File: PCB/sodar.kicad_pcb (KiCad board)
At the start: 2 copper layers, 71 parts, among them J1 Screw_Terminal_01x02, J2 Conn_02x12_Counter_Clockwise, J3 Conn_01x02, U1 TC78H621FNG, U10 TC78H621FNG, U2 TC78H621FNG, U3 TC78H621FNG, U4 TC78H621FNG, U5 TC78H621FNG, U6 TC78H621FNG, U7 TC78H621FNG, U8 TC78H621FNG, U9 TC78H621FNG

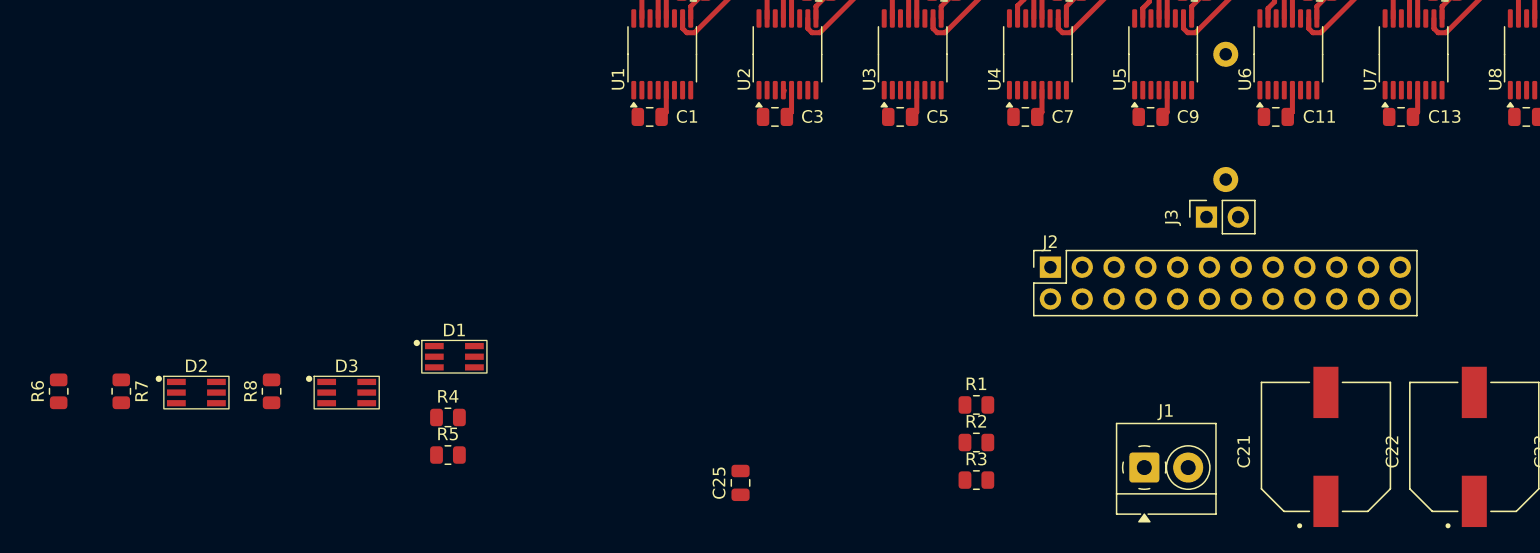
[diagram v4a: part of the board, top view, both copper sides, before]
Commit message: Moved signal connections on the header for easier routing
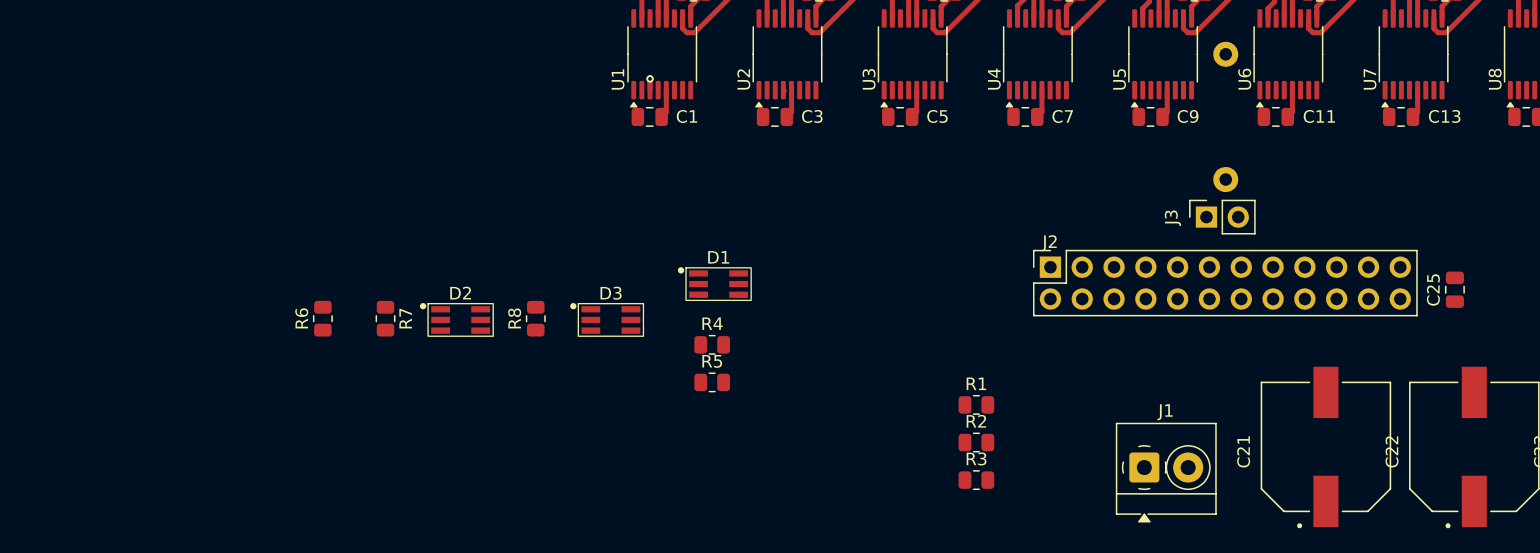
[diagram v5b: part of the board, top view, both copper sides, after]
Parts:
- moved C25 59.1 mm to (168.3, 71.8)
- moved D2 21.9 mm to (88.9, 72.1)
- moved D3 21.9 mm to (100.9, 72.1)
- moved R6 21.9 mm to (77.9, 74.1)
- moved R7 21.9 mm to (82.9, 74.1)
- moved R8 21.9 mm to (94.9, 74.1)
- moved D1 21.9 mm to (109.5, 69.2)
- moved R4 21.9 mm to (109.0, 76.2)
- moved R5 21.9 mm to (109.0, 79.2)
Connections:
- J2 pad 1: S1 -> S2
- J2 pad 10: S10 -> S9
- J2 pad 11: S11 -> S12
- J2 pad 12: S12 -> S11
- J2 pad 13: S13 -> S14
- J2 pad 14: S14 -> S13
- J2 pad 15: S15 -> S16
- J2 pad 16: S16 -> S15
- J2 pad 17: S17 -> S18
- J2 pad 18: S18 -> S17
- J2 pad 2: S2 -> S1
- J2 pad 3: S3 -> S4
- J2 pad 4: S4 -> S3
- J2 pad 5: S5 -> S6
- J2 pad 6: S6 -> S5
- J2 pad 7: S7 -> S8
- J2 pad 8: S8 -> S7
- J2 pad 9: S9 -> S10
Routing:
- net S1: track 0.00 -> 0.90 mm, vias 0 -> 1
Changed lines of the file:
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@@
 	(footprint "footprints:QBLP680-RGB1"
 		(layer "F.Cu")
-		(at 88.4 75.05)
+		(at 109.5 69.25)
 		(property "Reference" "D1"
 			(at 0 0 0)
@@
 	(footprint "Resistor_SMD:R_0805_2012Metric"
 		(layer "F.Cu")
-		(at 56.8 79.9125 90)
+		(at 77.9 74.1125 90)
 		(descr "Resistor SMD 0805 (2012 Metric), square (rectangular) end terminal, IPC_7351 nominal, (Body size source: IPC-SM-782 page 72, https://www.pcb-3d.com/wordpress/wp-content/uploads/ipc-sm-782a_amendment_1_and_2.pdf), generated with kicad-footprint-generator")
 		(tags "resistor")
@@
 	(footprint "Resistor_SMD:R_0805_2012Metric"
 		(layer "F.Cu")
-		(at 61.8 79.9125 -90)
+		(at 82.9 74.1125 -90)
 		(descr "Resistor SMD 0805 (2012 Metric), square (rectangular) end terminal, IPC_7351 nominal, (Body size source: IPC-SM-782 page 72, https://www.pcb-3d.com/wordpress/wp-content/uploads/ipc-sm-782a_amendment_1_and_2.pdf), generated with kicad-footprint-generator")
 		(tags "resistor")
@@
 	(footprint "footprints:QBLP680-RGB1"
 		(layer "F.Cu")
-		(at 79.8 77.9125)
+		(at 100.9 72.1125)
 		(property "Reference" "D3"
 			(at 0 0 0)
@@
 	(footprint "Resistor_SMD:R_0805_2012Metric"
 		(layer "F.Cu")
-		(at 87.8875 82)
+		(at 108.9875 76.2)
 		(descr "Resistor SMD 0805 (2012 Metric), square (rectangular) end terminal, IPC_7351 nominal, (Body size source: IPC-SM-782 page 72, https://www.pcb-3d.com/wordpress/wp-content/uploads/ipc-sm-782a_amendment_1_and_2.pdf), generated with kicad-footprint-generator")
 		(tags "resistor")
@@
 	(footprint "Resistor_SMD:R_0805_2012Metric"
 		(layer "F.Cu")
-		(at 87.8875 85)
+		(at 108.9875 79.2)
 		(descr "Resistor SMD 0805 (2012 Metric), square (rectangular) end terminal, IPC_7351 nominal, (Body size source: IPC-SM-782 page 72, https://www.pcb-3d.com/wordpress/wp-content/uploads/ipc-sm-782a_amendment_1_and_2.pdf), generated with kicad-footprint-generator")
 		(tags "resistor")
@@
 	(footprint "Resistor_SMD:R_0805_2012Metric"
 		(layer "F.Cu")
-		(at 73.8 79.9125 90)
+		(at 94.9 74.1125 90)
 		(descr "Resistor SMD 0805 (2012 Metric), square (rectangular) end terminal, IPC_7351 nominal, (Body size source: IPC-SM-782 page 72, https://www.pcb-3d.com/wordpress/wp-content/uploads/ipc-sm-782a_amendment_1_and_2.pdf), generated with kicad-footprint-generator")
 		(tags "resistor")
@@
 	(footprint "Capacitor_SMD:C_0805_2012Metric"
 		(layer "F.Cu")
-		(at 111.25 87.225 90)
+		(at 168.3 71.8 90)
 		(descr "Capacitor SMD 0805 (2012 Metric), square (rectangular) end terminal, IPC_7351 nominal, (Body size source: IPC-SM-782 page 76, https://www.pcb-3d.com/wordpress/wp-content/uploads/ipc-sm-782a_amendment_1_and_2.pdf, https://docs.google.com/spreadsheets/d/1BsfQQcO9C6DZCsRaXUlFlo91Tg2WpOkGARC1WS5S8t0/edit?usp=sharing), generated with kicad-footprint-generator")
 		(tags "capacitor")
@@
 			(layers "*.Cu" "*.Mask")
 			(remove_unused_layers no)
-			(net 39 "S1")
+			(net 35 "S2")
 			(pinfunction "Pin_1")
 			(pintype "passive")
@@
 			(layers "*.Cu" "*.Mask")
 			(remove_unused_layers no)
-			(net 35 "S2")
+			(net 39 "S1")
 			(pinfunction "Pin_2")
 			(pintype "passive")
@@
 			(layers "*.Cu" "*.Mask")
 			(remove_unused_layers no)
-			(net 42 "S3")
+			(net 38 "S4")
 			(pinfunction "Pin_3")
 			(pintype "passive")
@@
 			(layers "*.Cu" "*.Mask")
 			(remove_unused_layers no)
-			(net 38 "S4")
+			(net 42 "S3")
 			(pinfunction "Pin_4")
 			(pintype "passive")
@@
 			(layers "*.Cu" "*.Mask")
 			(remove_unused_layers no)
-			(net 32 "S5")
+			(net 29 "S6")
 			(pinfunction "Pin_5")
 			(pintype "passive")
@@
 			(layers "*.Cu" "*.Mask")
 			(remove_unused_layers no)
-			(net 29 "S6")
+			(net 32 "S5")
 			(pinfunction "Pin_6")
 			(pintype "passive")
@@
 			(layers "*.Cu" "*.Mask")
 			(remove_unused_layers no)
-			(net 28 "S7")
+			(net 25 "S8")
 			(pinfunction "Pin_7")
 			(pintype "passive")
@@
 			(layers "*.Cu" "*.Mask")
 			(remove_unused_layers no)
-			(net 25 "S8")
+			(net 28 "S7")
 			(pinfunction "Pin_8")
 			(pintype "passive")
@@
 			(layers "*.Cu" "*.Mask")
 			(remove_unused_layers no)
-			(net 36 "S9")
+			(net 26 "S10")
 			(pinfunction "Pin_9")
 			(pintype "passive")
@@
 			(layers "*.Cu" "*.Mask")
 			(remove_unused_layers no)
-			(net 26 "S10")
+			(net 36 "S9")
 			(pinfunction "Pin_10")
 			(pintype "passive")
@@
 			(layers "*.Cu" "*.Mask")
 			(remove_unused_layers no)
-			(net 40 "S11")
+			(net 34 "S12")
 			(pinfunction "Pin_11")
 			(pintype "passive")
@@
 			(layers "*.Cu" "*.Mask")
 			(remove_unused_layers no)
-			(net 34 "S12")
+			(net 40 "S11")
 			(pinfunction "Pin_12")
 			(pintype "passive")
@@
 			(layers "*.Cu" "*.Mask")
 			(remove_unused_layers no)
-			(net 41 "S13")
+			(net 33 "S14")
 			(pinfunction "Pin_13")
 			(pintype "passive")
@@
 			(layers "*.Cu" "*.Mask")
 			(remove_unused_layers no)
-			(net 33 "S14")
+			(net 41 "S13")
 			(pinfunction "Pin_14")
 			(pintype "passive")
@@
 			(layers "*.Cu" "*.Mask")
 			(remove_unused_layers no)
-			(net 37 "S15")
+			(net 43 "S16")
 			(pinfunction "Pin_15")
 			(pintype "passive")
@@
 			(layers "*.Cu" "*.Mask")
 			(remove_unused_layers no)
-			(net 43 "S16")
+			(net 37 "S15")
 			(pinfunction "Pin_16")
 			(pintype "passive")
@@
 			(layers "*.Cu" "*.Mask")
 			(remove_unused_layers no)
-			(net 30 "S17")
+			(net 27 "S18")
 			(pinfunction "Pin_17")
 			(pintype "passive")
@@
 			(layers "*.Cu" "*.Mask")
 			(remove_unused_layers no)
-			(net 27 "S18")
+			(net 30 "S17")
 			(pinfunction "Pin_18")
 			(pintype "passive")
@@
 	(footprint "footprints:QBLP680-RGB1"
 		(layer "F.Cu")
-		(at 67.8 77.9125)
+		(at 88.9 72.1125)
 		(property "Reference" "D2"
 			(at 0 0 0)
@@
 	)
 	(segment
+		(start 104.025 54.971)
+		(end 104.033551 54.962449)
+		(width 0.4)
+		(layer "F.Cu")
+		(net 39)
+	)
+	(segment
+		(start 104.025 55.8625)
+		(end 104.025 54.971)
+		(width 0.4)
+		(layer "F.Cu")
+		(net 39)
+	)
+	(via
+		(at 104.025 54.962449)
+		(size 0.6)
+		(drill 0.3)
+		(layers "F.Cu" "B.Cu")
+		(net 39)
+	)
+	(segment

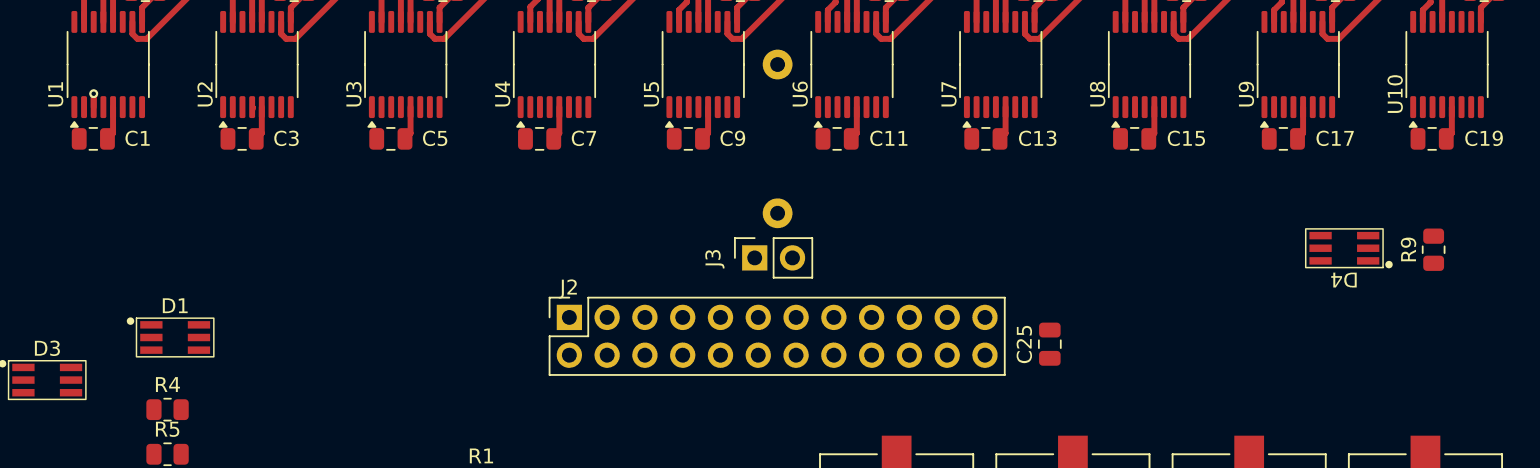
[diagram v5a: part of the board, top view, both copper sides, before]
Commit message: Routed signal lines from the headero to the driver ICs
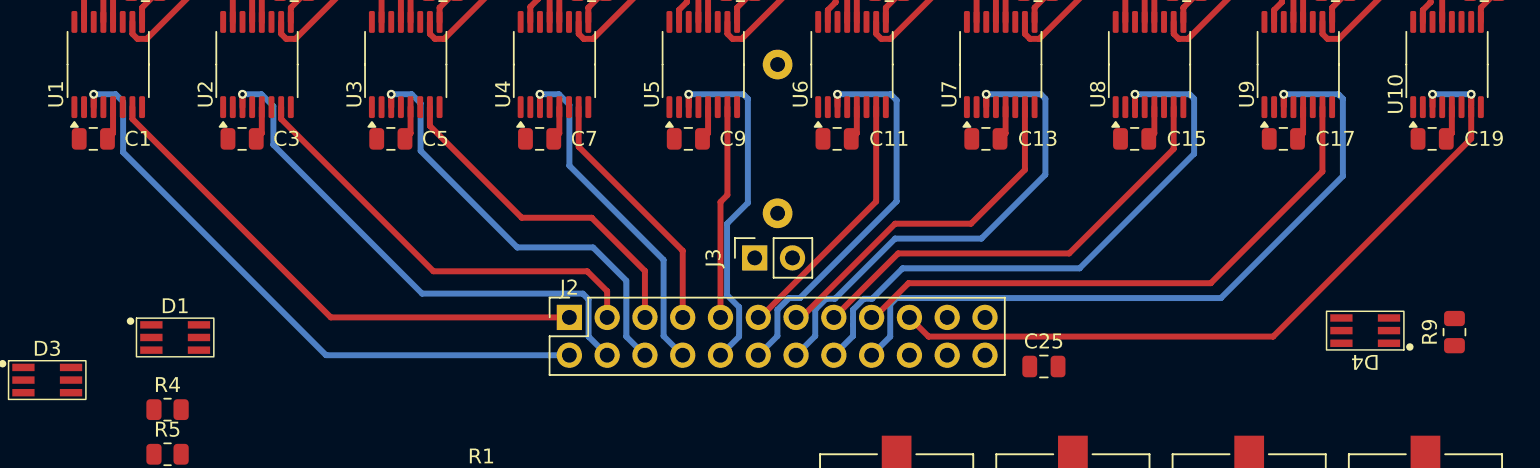
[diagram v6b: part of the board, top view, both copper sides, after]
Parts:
- moved D4 5.71 mm to (189.5, 73.0)
- moved R9 5.71 mm to (195.5, 71.0)
- moved C25 1.55 mm to (167.9, 73.3), turned to 0 degrees
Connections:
- U6 pad 2: unconnected-(U6-NC-Pad2) -> S11
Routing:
- net S19: track 0.00 -> 50.3 mm, vias 0 -> 2
- net S17: track 0.00 -> 48.2 mm, vias 0 -> 1
- net S1: track 0.90 -> 42.1 mm
- net S15: track 0.00 -> 39.5 mm, vias 0 -> 1
- net S18: track 0.00 -> 38.7 mm
- net S2: track 0.00 -> 35.7 mm
- net S3: track 0.00 -> 35.7 mm, vias 0 -> 1
- net S13: track 0.00 -> 32.8 mm, vias 0 -> 1
- net S16: track 0.00 -> 30.3 mm
- net S5: track 0.00 -> 29.4 mm, vias 0 -> 1
- net S4: track 0.00 -> 29.3 mm
- net S11: track 0.00 -> 26.5 mm, vias 0 -> 1
- net S14: track 0.00 -> 23.7 mm
- net S9: track 0.00 -> 23.7 mm, vias 0 -> 1
- net S7: track 0.00 -> 23.2 mm, vias 0 -> 1
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
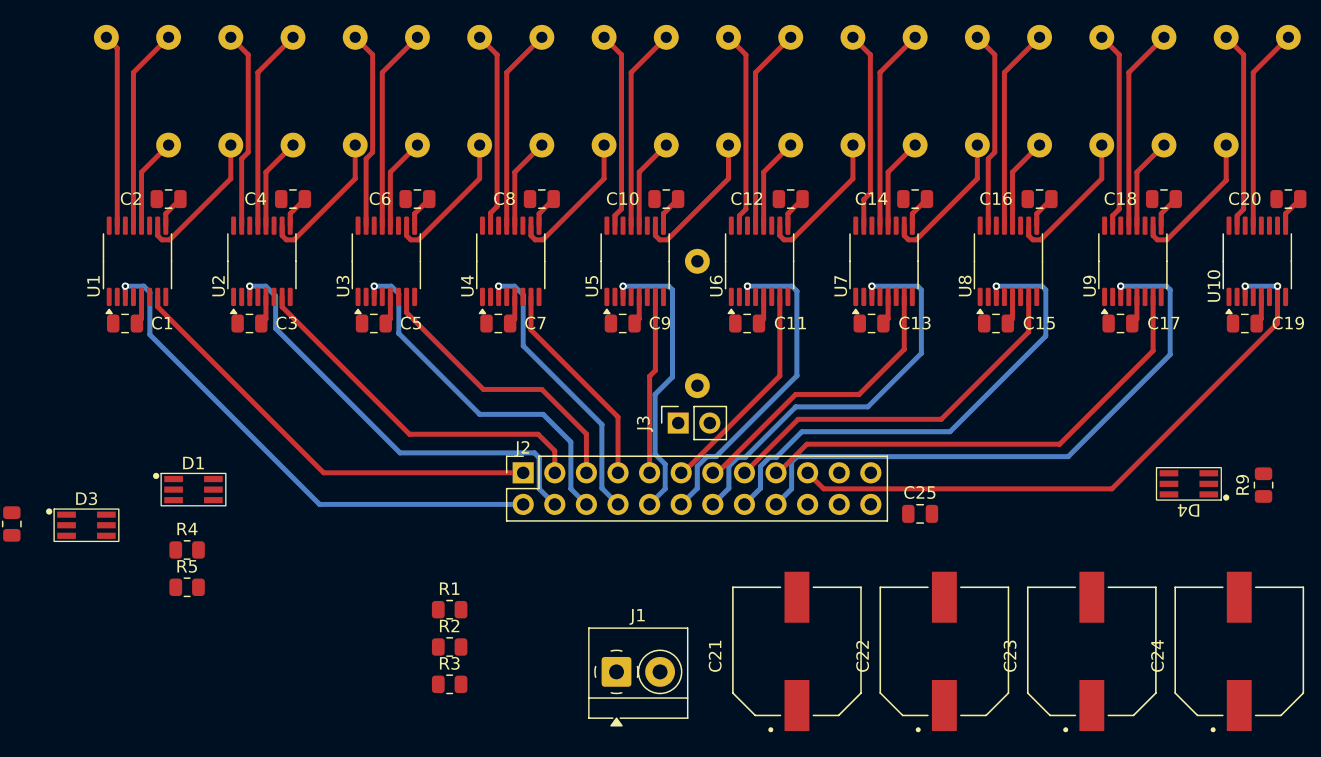
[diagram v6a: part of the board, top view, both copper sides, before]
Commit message: Improved signal routing & routed receiver pull-down resistors
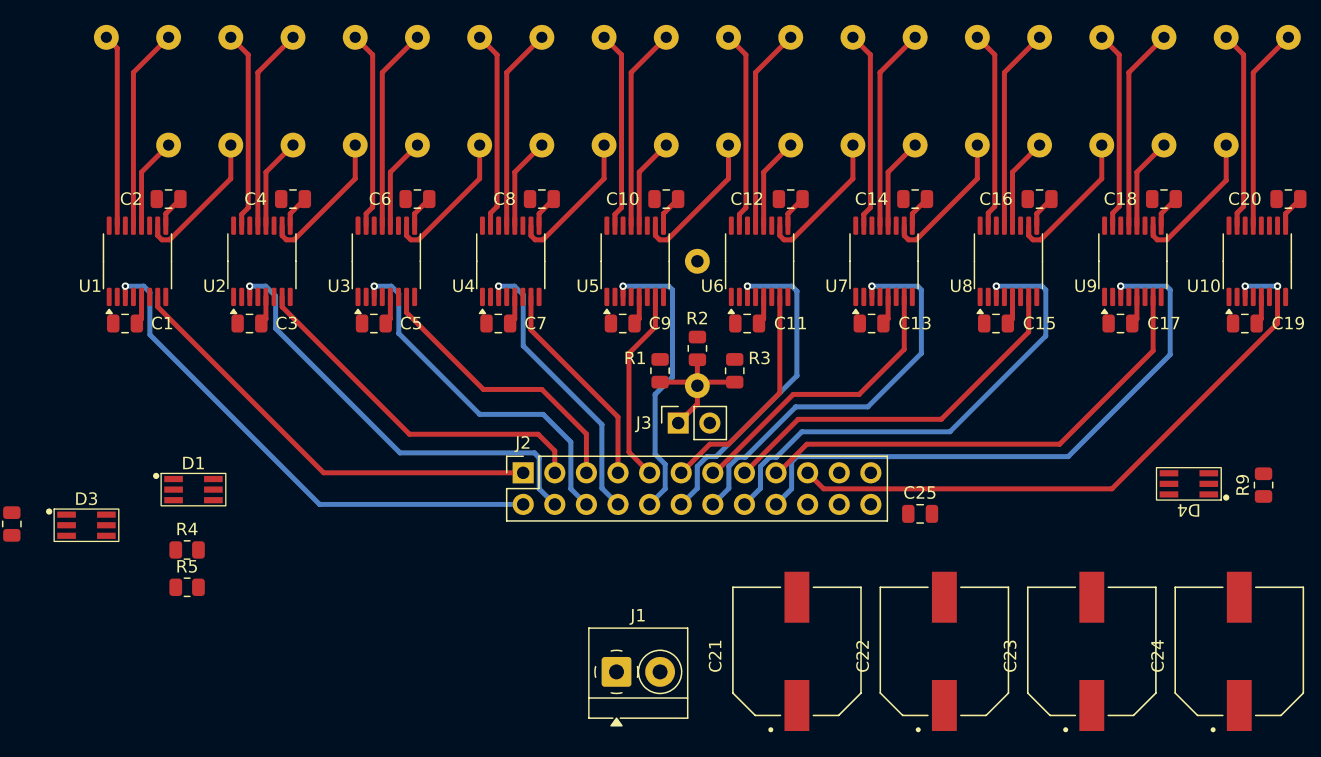
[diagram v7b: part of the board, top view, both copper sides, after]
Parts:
- moved R3 34.1 mm to (153.0, 61.8), turned to 90 degrees
- moved R2 31.2 mm to (150.0, 60.0), turned to 90 degrees
- moved R1 25.6 mm to (147.0, 61.8), turned to 90 degrees
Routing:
- net RX: track 0.00 -> 12.0 mm
- net S10: track 14.3 -> 15.7 mm
- net S12: track 17.5 -> 18.3 mm
